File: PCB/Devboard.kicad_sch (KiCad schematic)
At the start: 33 parts, among them J1 USB_C_Receptacle_USB2.0_14P, J2 Conn_01x20, J3 Conn_01x20, J4 Conn_01x03, SW1 SW_Push, U1 RP2040, U2 MCP1700x-330xxTT, U3 W25Q16JVSS, Y1 12 MHz

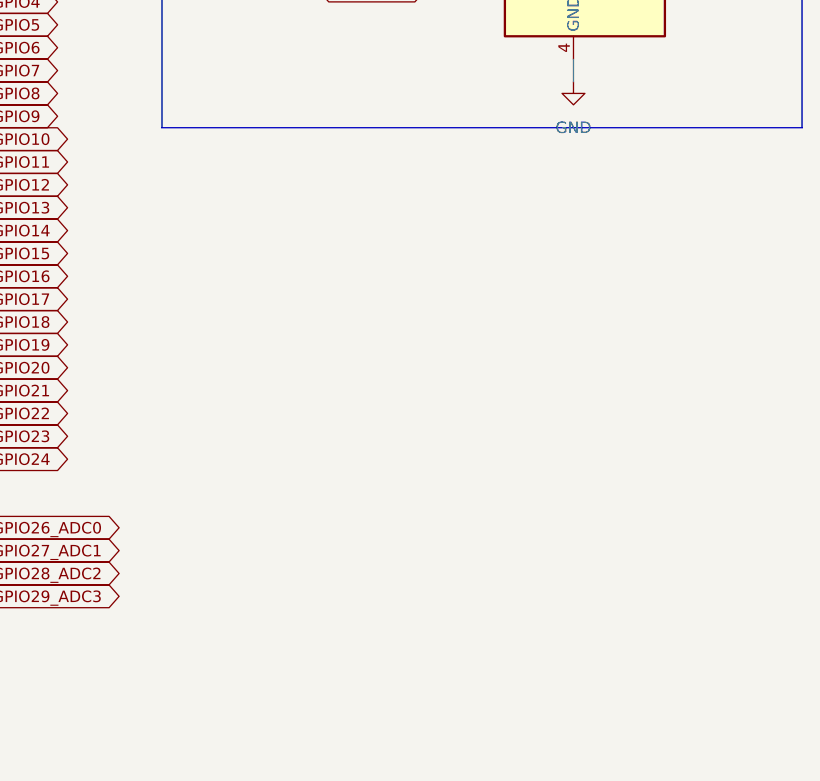
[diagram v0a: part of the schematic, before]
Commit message: added LEDs
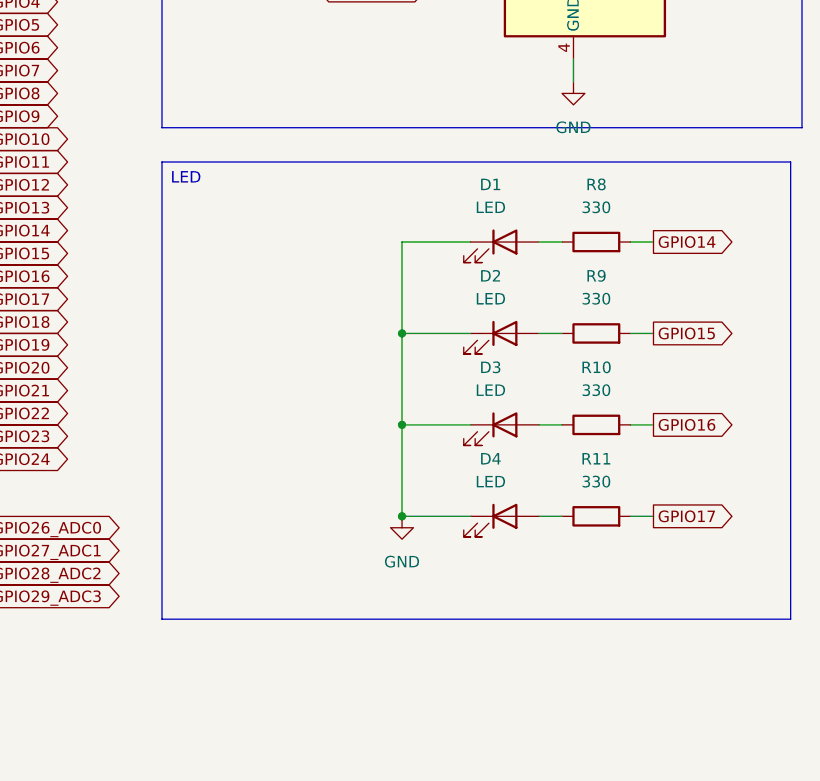
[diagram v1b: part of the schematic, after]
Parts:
- added D1, D2, D3, D4: LED, LED_SMD:LED_0603_1608Metric, symbol Device:LED
- added R10, R11, R8, R9: 330, Resistor_SMD:R_0603_1608Metric, symbol Device:R
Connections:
- net GND: now also D1.1 (K), D2.1 (K), D3.1 (K), D4.1 (K)
- net GPIO14: now also R8.2
- net GPIO15: now also R9.2
- net GPIO16: now also R10.2
- net GPIO17: now also R11.2
- new net: D1.2 (A), R8.1
- new net: D2.2 (A), R9.1
- new net: D3.2 (A), R10.1
- new net: D4.2 (A), R11.1
